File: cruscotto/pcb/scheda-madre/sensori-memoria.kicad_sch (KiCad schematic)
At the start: 13 parts, among them J6 STEVAL-MKI196V1 (DIL-24), J7 MicroSD, U10 DS3231SN

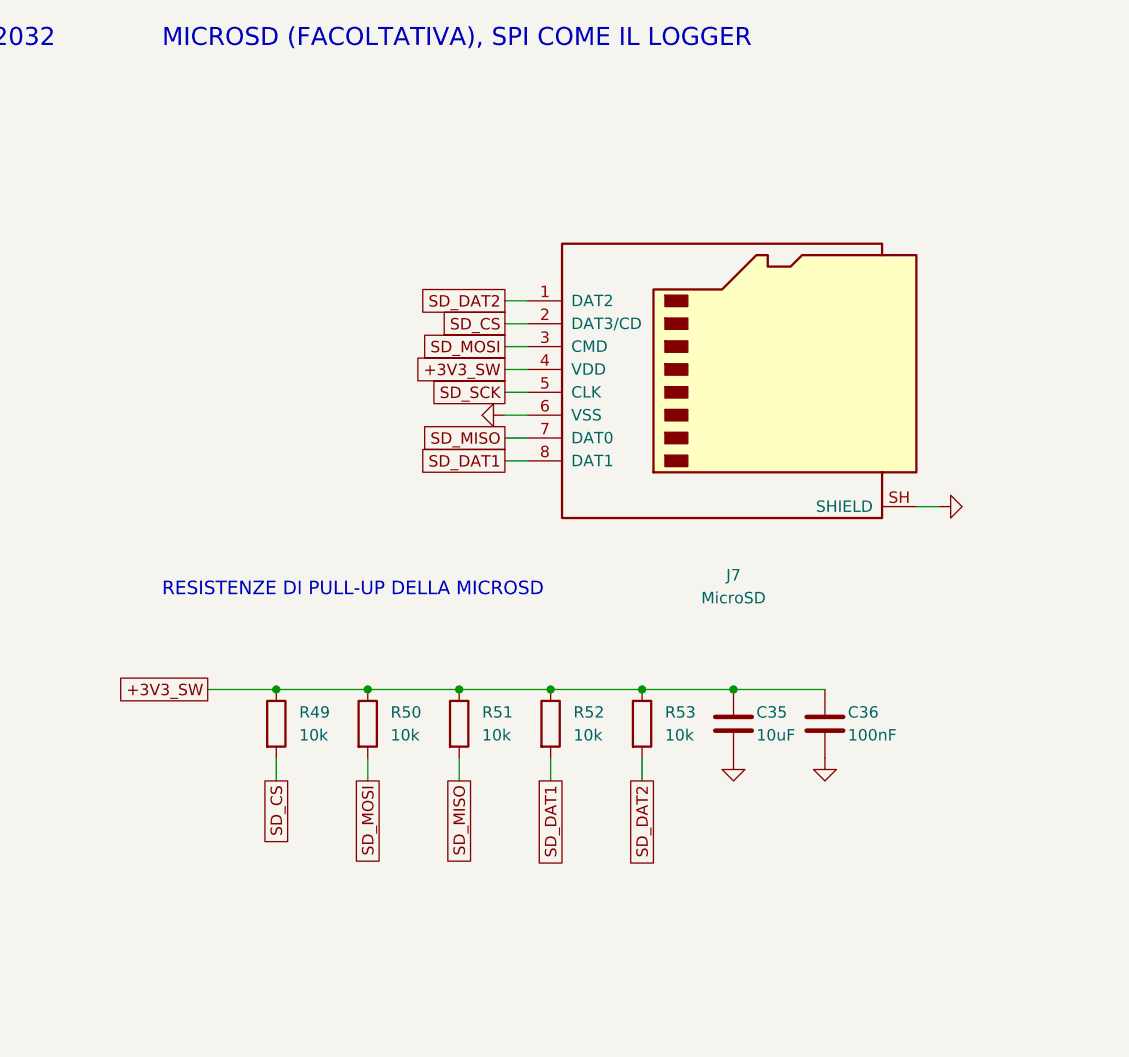
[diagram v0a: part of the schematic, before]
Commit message: feat(schematic): D-051 mixed approach, VAN and MicroSD as modules on pin headers, RTC stays a chip
CR-EL-003 rev B: blue SN65HVD230 module on J8/J9 headers with TX tied high on the board, NUP2105L kept. CR-EL-004 rev B: MicroSD reader module on a 6-way header, CS pull-up and bulk caps. Inventory: second module units needed for the mainboard, header spacing to measure. ERC: 0 errors; 88 nets checked.

Co-Authored-By: Claude Opus 5.5 <noreply@anthropic.com>
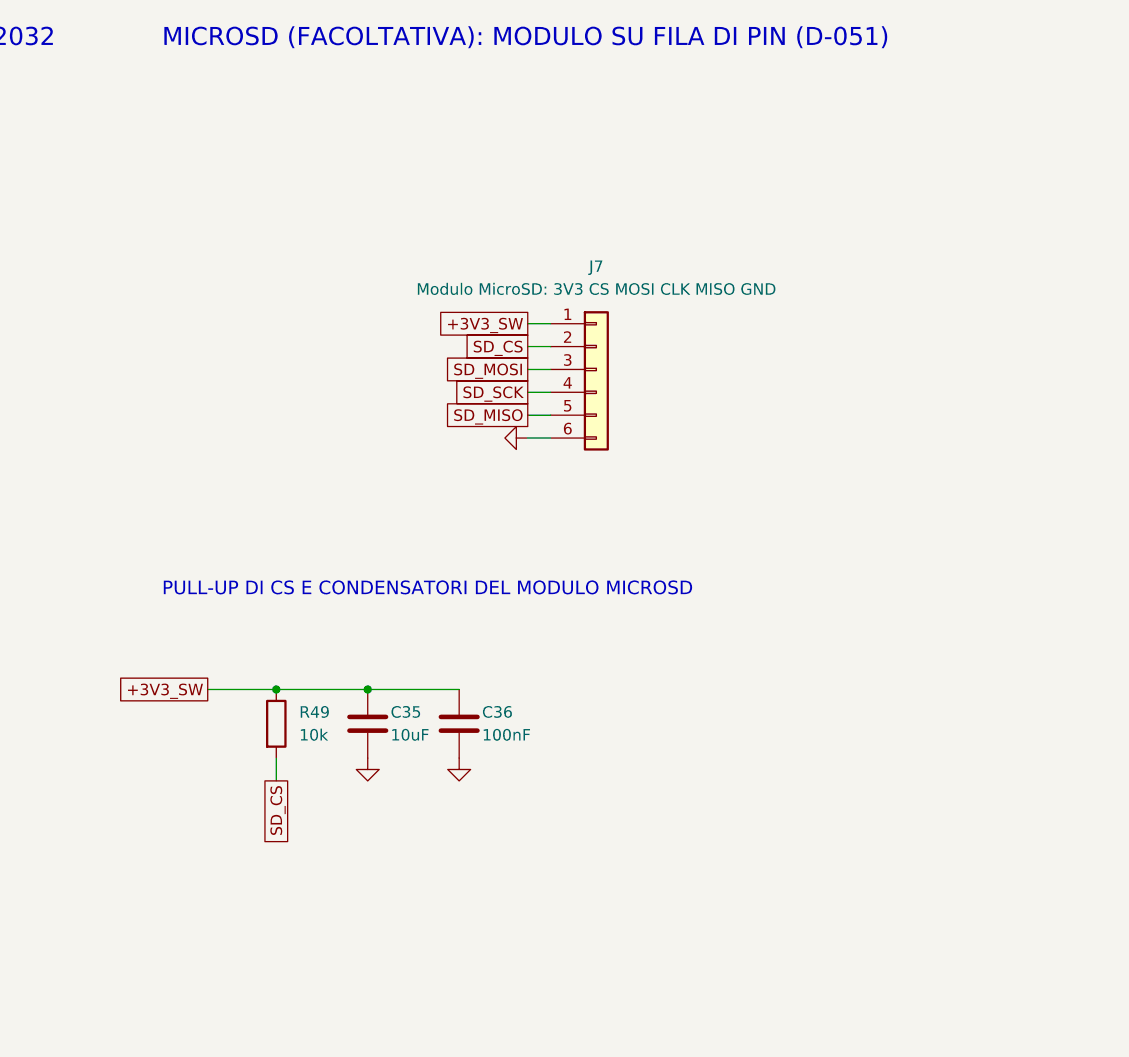
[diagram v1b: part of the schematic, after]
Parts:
- removed R50, R51, R52, R53: 10k, Resistor_SMD:R_0805_2012Metric_Pad1.20x1.40mm_HandSolder, symbol Device:R
- J7: value MicroSD -> Modulo MicroSD: 3V3 CS MOSI CLK MISO GND; footprint Connector_Card:microSD_HC_Hirose_DM3AT-SF-PEJM5 -> Connector_PinHeader_2.54mm:PinHeader_1x06_P2.54mm_Vertical; symbol Connector:Micro_SD_Card -> Connector_Generic:Conn_01x06
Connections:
- net SD_DAT2 is gone; now on net +3V3_SW: J7.1 (Pin_1)
- net +3V3_SW: no longer J7.4 (VDD)
- net GND: no longer J7.SH (SHIELD)
- net SD_MISO: now also J7.5 (Pin_5); no longer J7.7 (DAT0)
- net SD_SCK: now also J7.4 (Pin_4); no longer J7.5 (CLK)
- removed net SD_DAT1: J7.8 (DAT1)
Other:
- note added: "MICROSD (FACOLTATIVA): MODULO SU FILA DI PIN (D-051)"
- note added: "PULL-UP DI CS E CONDENSATORI DEL MODULO MICROSD"
- note removed: "MICROSD (FACOLTATIVA), SPI COME IL LOGGER"
- note removed: "RESISTENZE DI PULL-UP DELLA MICROSD"
- moved on the sheet: C35, C36

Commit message: feat(pcb): ST DIL24 adapter footprint (15.0 mm row spacing) from ST Gerbers; IMU socket uses it
Board 18.0 x 30.5 mm, 2x12 pins at 2.54 mm, rows 15.0 mm apart, pin 1 top-left. Inventory HW-IMU-LSM6DSO updated; project footprint library with fp-lib-table.

Co-Authored-By: Claude Opus 5.5 <noreply@anthropic.com>
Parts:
- J6: footprint Package_DIP:DIP-24_W15.24mm_Socket -> scheda-madre:ST_DIL24_Adapter_W15.0mm
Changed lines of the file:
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@@
 		(property "Reference" "J6" (at 60.96 69.85 0) (effects (font (size 1.27 1.27))))
 		(property "Value" "STEVAL-MKI196V1 (DIL-24)" (at 60.96 72.39 0) (effects (font (size 1.27 1.27))))
-		(property "Footprint" "Package_DIP:DIP-24_W15.24mm_Socket" (at 60.96 88.9 0) (hide yes) (effects (font (size 1.27 1.27))))
+		(property "Footprint" "scheda-madre:ST_DIL24_Adapter_W15.0mm" (at 60.96 88.9 0) (hide yes) (effects (font (size 1.27 1.27))))
 		(property "Datasheet" "" (at 60.96 88.9 0) (hide yes) (effects (font (size 1.27 1.27))))
-		(property "Description" "HW-IMU-LSM6DSO; piedinatura da ST DB3714 rev 1, da riscontrare sulla serigrafia all’arrivo" (at 60.96 88.9 0) (hide yes) (effects (font (size 1.27 1.27))))
+		(property "Description" "HW-IMU-LSM6DSO; piedinatura ST DB3714 rev 1; file di pin a 15,0 mm (Gerber ST), due strip femmina 1x12" (at 60.96 88.9 0) (hide yes) (effects (font (size 1.27 1.27))))
 		(pin "1")
 		(pin "2")

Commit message: feat(schematic): D-056 RTC without coin cell, DS3231 on the always-on 3.3 V with VBAT grounded
BT1 removed from schematic and placement list; PCB regenerated after the routing run in progress.

Co-Authored-By: Claude Opus 5.5 <noreply@anthropic.com>
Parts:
- removed BT1: CR2032, Battery:BatteryHolder_Keystone_3034_1x20mm, symbol Device:Battery_Cell
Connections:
- net GND: now also U10.14 (VBAT)
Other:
- note added: "IMU e RTC sul 3,3 V sempre acceso (consumi a riposo di pochi uA); MicroSD sul 3,3 V acceso a quadro. RTC senza pila (D-056): ora persa solo staccando la batteria dell’auto."
- note added: "RTC DS3231SN (FACOLTATIVO) SENZA PILA (D-056)"
- note removed: "IMU e RTC sul 3,3 V sempre acceso (consumi a riposo di pochi uA); MicroSD sul 3,3 V acceso a quadro. Pila dell’RTC non ricaricata (D-019)."
- note removed: "RTC DS3231SN (FACOLTATIVO) CON CR2032"
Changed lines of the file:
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@@
 	(global_label "+3V3_AON" (shape passive) (at 147.32 63.5 180) (fields_autoplaced yes) (effects (font (size 1.27 1.27)) (justify right))
 		(property "Intersheetrefs" "${INTERSHEET_REFS}" (at 147.32 63.5 0) (effects (font (size 1.27 1.27)) (justify right) (hide yes))))
-	(symbol (lib_id "Device:Battery_Cell") (at 175.26 71.12 0) (unit 1) (exclude_from_sim no) (in_bom yes) (on_board yes) (dnp no)
-		(property "Reference" "BT1" (at 177.8 69.85 0) (effects (font (size 1.27 1.27)) (justify left)))
-		(property "Value" "CR2032" (at 177.8 72.39 0) (effects (font (size 1.27 1.27)) (justify left)))
-		(property "Footprint" "Battery:BatteryHolder_Keystone_3034_1x20mm" (at 175.26 71.12 0) (hide yes) (effects (font (size 1.27 1.27))))
-		(property "Datasheet" "" (at 175.26 71.12 0) (hide yes) (effects (font (size 1.27 1.27))))
-		(property "Description" "HW-RTC-BATTERY, da procurare" (at 175.26 71.12 0) (hide yes) (effects (font (size 1.27 1.27))))
-		(pin "1")
-		(pin "2")
-		(instances (project "scheda-madre" (path "/ccee1fe6-cbff-5665-be3b-629f18d22eb3/d397dd4f-6a73-5b5c-8d15-f0483e1efe4f" (reference "BT1") (unit 1))))
-	)
-	(symbol (lib_id "power:GND") (at 175.26 73.66 0) (unit 1) (exclude_from_sim no) (in_bom no) (on_board no) (dnp no)
-		(property "Reference" "#PWR087" (at 175.26 67.31 0) (hide yes) (effects (font (size 1.27 1.27))))
-		(property "Value" "GND" (at 175.26 69.85 0) (hide yes) (effects (font (size 1.27 1.27))))
-		(property "Footprint" "" (at 175.26 73.66 0) (hide yes) (effects (font (size 1.27 1.27))))
-		(property "Datasheet" "" (at 175.26 73.66 0) (hide yes) (effects (font (size 1.27 1.27))))
-		(property "Description" "" (at 175.26 73.66 0) (hide yes) (effects (font (size 1.27 1.27))))
+	(wire (pts (xy 165.1 71.12) (xy 165.1 68.58)) (stroke (width 0) (type default)))
+	(symbol (lib_id "power:GND") (at 165.1 68.58 180) (unit 1) (exclude_from_sim no) (in_bom no) (on_board no) (dnp no)
+		(property "Reference" "#PWR087" (at 165.1 62.23 0) (hide yes) (effects (font (size 1.27 1.27))))
+		(property "Value" "GND" (at 165.1 64.77 0) (hide yes) (effects (font (size 1.27 1.27))))
+		(property "Footprint" "" (at 165.1 68.58 0) (hide yes) (effects (font (size 1.27 1.27))))
+		(property "Datasheet" "" (at 165.1 68.58 0) (hide yes) (effects (font (size 1.27 1.27))))
+		(property "Description" "" (at 165.1 68.58 0) (hide yes) (effects (font (size 1.27 1.27))))
 		(pin "1")
 		(instances (project "scheda-madre" (path "/ccee1fe6-cbff-5665-be3b-629f18d22eb3/d397dd4f-6a73-5b5c-8d15-f0483e1efe4f" (reference "#PWR087") (unit 1))))
-	)
-	(wire (pts (xy 165.1 71.12) (xy 165.1 66.04)) (stroke (width 0) (type default)))
-	(wire (pts (xy 165.1 66.04) (xy 175.26 66.04)) (stroke (width 0) (type default)))
-	(symbol (lib_id "power:PWR_FLAG") (at 165.1 66.04 0) (unit 1) (exclude_from_sim no) (in_bom no) (on_board no) (dnp no)
-		(property "Reference" "#FLG088" (at 165.1 59.69 0) (hide yes) (effects (font (size 1.27 1.27))))
-		(property "Value" "PWR_FLAG" (at 165.1 62.23 0) (hide yes) (effects (font (size 1.27 1.27))))
-		(property "Footprint" "" (at 165.1 66.04 0) (hide yes) (effects (font (size 1.27 1.27))))
-		(property "Datasheet" "" (at 165.1 66.04 0) (hide yes) (effects (font (size 1.27 1.27))))
-		(property "Description" "" (at 165.1 66.04 0) (hide yes) (effects (font (size 1.27 1.27))))
-		(pin "1")
-		(instances (project "scheda-madre" (path "/ccee1fe6-cbff-5665-be3b-629f18d22eb3/d397dd4f-6a73-5b5c-8d15-f0483e1efe4f" (reference "#FLG088") (unit 1))))
 	)
 	(symbol (lib_id "Connector_Generic:Conn_01x06") (at 264.16 81.28 0) (unit 1) (exclude_from_sim no) (in_bom yes) (on_board yes) (dnp no)
@@
 	(wire (pts (xy 259.08 88.9) (xy 256.54 88.9)) (stroke (width 0) (type default)))
 	(symbol (lib_id "power:GND") (at 256.54 88.9 270) (unit 1) (exclude_from_sim no) (in_bom no) (on_board no) (dnp no)
-		(property "Reference" "#PWR089" (at 256.54 82.55 90) (hide yes) (effects (font (size 1.27 1.27))))
+		(property "Reference" "#PWR088" (at 256.54 82.55 90) (hide yes) (effects (font (size 1.27 1.27))))
 		(property "Value" "GND" (at 256.54 85.09 90) (hide yes) (effects (font (size 1.27 1.27))))
 		(property "Footprint" "" (at 256.54 88.9 0) (hide yes) (effects (font (size 1.27 1.27))))
@@
 		(property "Description" "" (at 256.54 88.9 0) (hide yes) (effects (font (size 1.27 1.27))))
 		(pin "1")
-		(instances (project "scheda-madre" (path "/ccee1fe6-cbff-5665-be3b-629f18d22eb3/d397dd4f-6a73-5b5c-8d15-f0483e1efe4f" (reference "#PWR089") (unit 1))))
+		(instances (project "scheda-madre" (path "/ccee1fe6-cbff-5665-be3b-629f18d22eb3/d397dd4f-6a73-5b5c-8d15-f0483e1efe4f" (reference "#PWR088") (unit 1))))
 	)
 	(global_label "+3V3_SW" (shape passive) (at 220.98 116.84 180) (fields_autoplaced yes) (effects (font (size 1.27 1.27)) (justify right))
@@
 	)
 	(symbol (lib_id "power:GND") (at 238.76 124.46 0) (unit 1) (exclude_from_sim no) (in_bom no) (on_board no) (dnp no)
-		(property "Reference" "#PWR090" (at 238.76 118.11 0) (hide yes) (effects (font (size 1.27 1.27))))
+		(property "Reference" "#PWR089" (at 238.76 118.11 0) (hide yes) (effects (font (size 1.27 1.27))))
 		(property "Value" "GND" (at 238.76 120.65 0) (hide yes) (effects (font (size 1.27 1.27))))
 		(property "Footprint" "" (at 238.76 124.46 0) (hide yes) (effects (font (size 1.27 1.27))))
@@
 		(property "Description" "" (at 238.76 124.46 0) (hide yes) (effects (font (size 1.27 1.27))))
 		(pin "1")
-		(instances (project "scheda-madre" (path "/ccee1fe6-cbff-5665-be3b-629f18d22eb3/d397dd4f-6a73-5b5c-8d15-f0483e1efe4f" (reference "#PWR090") (unit 1))))
+		(instances (project "scheda-madre" (path "/ccee1fe6-cbff-5665-be3b-629f18d22eb3/d397dd4f-6a73-5b5c-8d15-f0483e1efe4f" (reference "#PWR089") (unit 1))))
 	)
 	(symbol (lib_id "Device:C") (at 248.92 120.65 0) (unit 1) (exclude_from_sim no) (in_bom yes) (on_board yes) (dnp no)
@@
 	)
 	(symbol (lib_id "power:GND") (at 248.92 124.46 0) (unit 1) (exclude_from_sim no) (in_bom no) (on_board no) (dnp no)
-		(property "Reference" "#PWR091" (at 248.92 118.11 0) (hide yes) (effects (font (size 1.27 1.27))))
+		(property "Reference" "#PWR090" (at 248.92 118.11 0) (hide yes) (effects (font (size 1.27 1.27))))
 		(property "Value" "GND" (at 248.92 120.65 0) (hide yes) (effects (font (size 1.27 1.27))))
 		(property "Footprint" "" (at 248.92 124.46 0) (hide yes) (effects (font (size 1.27 1.27))))
@@
 		(property "Description" "" (at 248.92 124.46 0) (hide yes) (effects (font (size 1.27 1.27))))
 		(pin "1")
-		(instances (project "scheda-madre" (path "/ccee1fe6-cbff-5665-be3b-629f18d22eb3/d397dd4f-6a73-5b5c-8d15-f0483e1efe4f" (reference "#PWR091") (unit 1))))
+		(instances (project "scheda-madre" (path "/ccee1fe6-cbff-5665-be3b-629f18d22eb3/d397dd4f-6a73-5b5c-8d15-f0483e1efe4f" (reference "#PWR090") (unit 1))))
 	)
 	(wire (pts (xy 220.98 116.84) (xy 228.6 116.84)) (stroke (width 0) (type default)))
@@
 	(text "IMU SU MODULO DIL-24 (D-033, D-046)" (exclude_from_sim no) (at 25.4 45.72 0) (effects (font (size 2.0 2.0)) (justify left bottom)))
 	(text "STEVAL-MKI196V1, LSM6DSO, I2C 0x6A" (exclude_from_sim no) (at 25.4 50.8 0) (effects (font (size 1.5 1.5)) (justify left bottom)))
-	(text "RTC DS3231SN (FACOLTATIVO) CON CR2032" (exclude_from_sim no) (at 142.24 45.72 0) (effects (font (size 2.0 2.0)) (justify left bottom)))
+	(text "RTC DS3231SN (FACOLTATIVO) SENZA PILA (D-056)" (exclude_from_sim no) (at 142.24 45.72 0) (effects (font (size 2.0 2.0)) (justify left bottom)))
 	(text "MICROSD (FACOLTATIVA): MODULO SU FILA DI PIN (D-051)" (exclude_from_sim no) (at 215.9 45.72 0) (effects (font (size 2.0 2.0)) (justify left bottom)))
 	(text "PULL-UP DI CS E CONDENSATORI DEL MODULO MICROSD" (exclude_from_sim no) (at 215.9 106.68 0) (effects (font (size 1.5 1.5)) (justify left bottom)))
 	(text "Proposta preliminare, non verificata. Pull-up I2C sul foglio del front-end. Piedinatura del modulo IMU da riscontrare sulla serigrafia all’arrivo (HW-IMU-LSM6DSO)." (exclude_from_sim no) (at 25.4 236.22 0) (effects (font (size 1.27 1.27)) (justify left bottom)))
-	(text "IMU e RTC sul 3,3 V sempre acceso (consumi a riposo di pochi uA); MicroSD sul 3,3 V acceso a quadro. Pila dell’RTC non ricaricata (D-019)." (exclude_from_sim no) (at 25.4 241.3 0) (effects (font (size 1.27 1.27)) (justify left bottom)))
+	(text "IMU e RTC sul 3,3 V sempre acceso (consumi a riposo di pochi uA); MicroSD sul 3,3 V acceso a quadro. RTC senza pila (D-056): ora persa solo staccando la batteria dell’auto." (exclude_from_sim no) (at 25.4 241.3 0) (effects (font (size 1.27 1.27)) (justify left bottom)))
 	(text "Etichette con lo stesso nome sono collegate, anche tra fogli diversi." (exclude_from_sim no) (at 25.4 246.38 0) (effects (font (size 1.27 1.27)) (justify left bottom)))
 	(junction (at 154.94 63.5) (diameter 0) (color 0 0 0 0))
-	(junction (at 165.1 66.04) (diameter 0) (color 0 0 0 0))
 	(junction (at 165.1 91.44) (diameter 0) (color 0 0 0 0))
 	(junction (at 228.6 116.84) (diameter 0) (color 0 0 0 0))
